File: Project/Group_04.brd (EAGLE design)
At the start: 100 x 80 mm, 29 parts, among them J1 POWER_JACKPTH_LOCK, U1 +12v

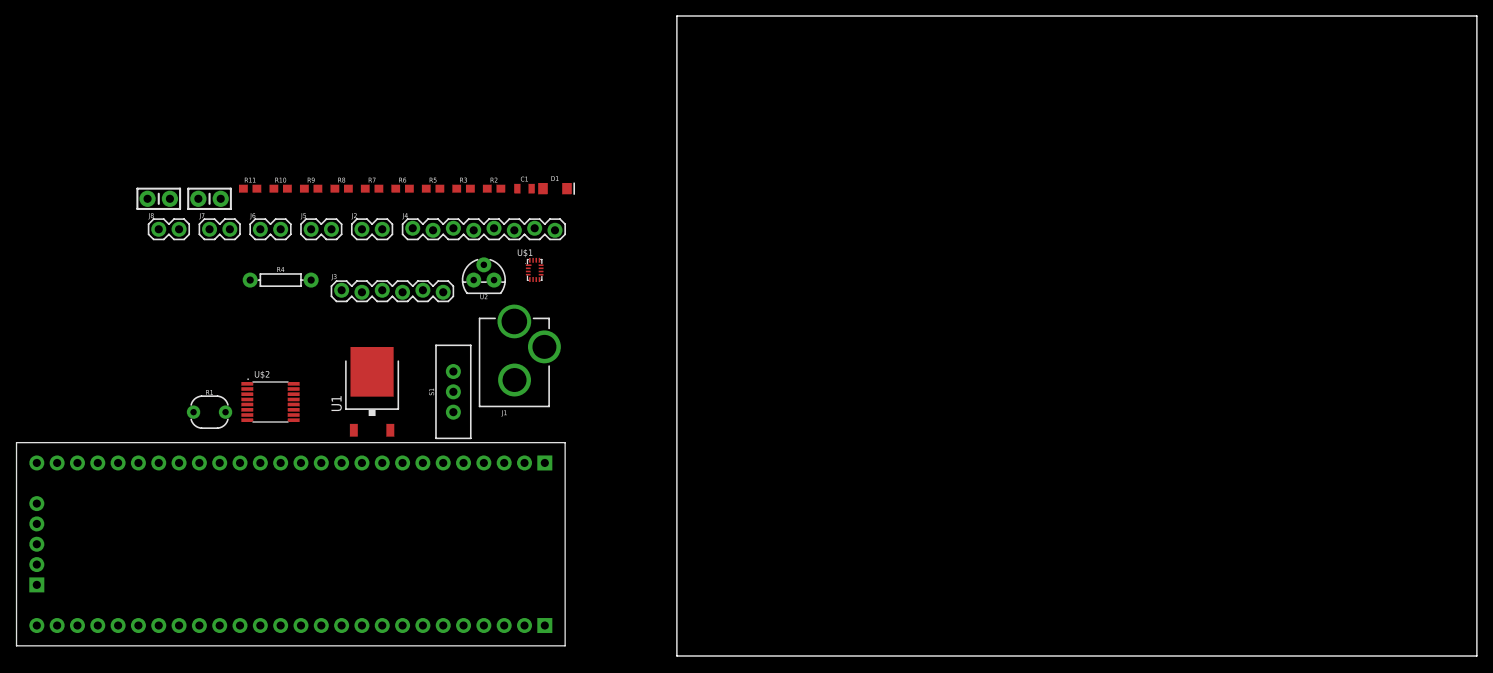
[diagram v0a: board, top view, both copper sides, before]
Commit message: components are positioned
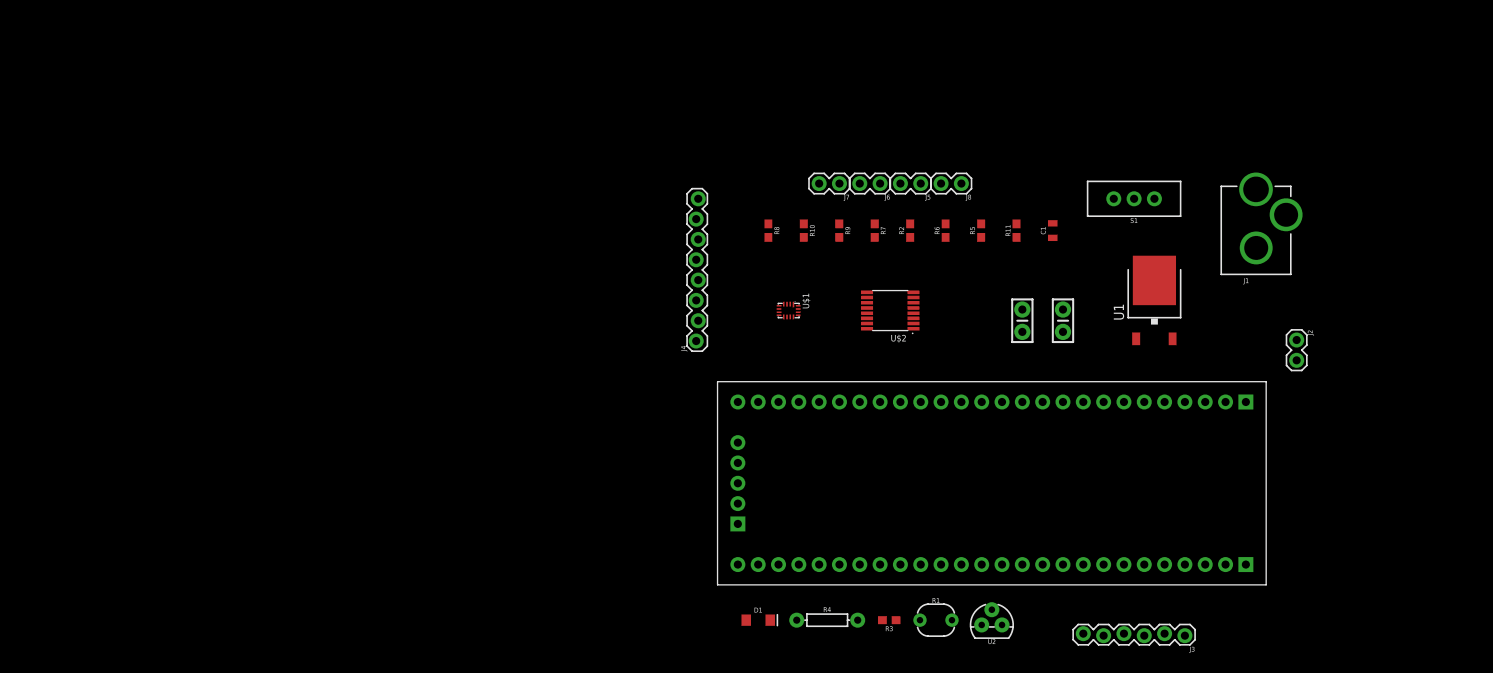
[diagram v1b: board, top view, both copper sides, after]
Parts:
- moved J2 117.7 mm to (77.5, 39.5), turned to 270 degrees
- moved C3 114.1 mm to (48.3, 41.9), turned to 270 degrees
- moved J3 113.9 mm to (63.5, 2.54), turned to 180 degrees
- moved C2 102.7 mm to (43.2, 41.9), turned to 270 degrees
- moved J8 100.5 mm to (35.6, 59.1), turned to 180 degrees
- moved U1 98.5 mm to (59.7, 44.5)
- moved R11 95.9 mm to (42.5, 53.2), turned to 90 degrees
- moved R1 94.5 mm to (32.4, 4.48)
- moved J1 94.2 mm to (72.4, 44.5)
- moved S1 88.4 mm to (57.1, 57.1), turned to 90 degrees
- moved U$3 88.0 mm to (40.6, 22.9)
- moved R4 80.5 mm to (18.8, 4.48)
- moved J7 78.9 mm to (20.3, 59.1), turned to 180 degrees
- moved U$2 78.3 mm to (26.7, 43.2), turned to 180 degrees
- moved J6 77.7 mm to (25.4, 59.1), turned to 180 degrees
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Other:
- board outline removed

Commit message: routed
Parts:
- moved U2 1.56 mm to (40.8, 4.44), turned to 90 degrees
- moved R4 0.96 mm to (19.7, 4.44)
- moved R3 0.76 mm to (27.3, 4.44), turned to 90 degrees
- moved R1 0.57 mm to (33.0, 4.44)
- moved D1 0.26 mm to (10.4, 4.44)
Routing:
- net 5V: track 0.00 -> 254.5 mm, vias 0 -> 2
- net I2C_A2: track 0.00 -> 34.9 mm
- net I2C_A0: track 0.00 -> 34.9 mm, vias 0 -> 2
- net I2C_A1: track 0.00 -> 31.9 mm
- net I2C_SCL_3: track 0.00 -> 30.9 mm, vias 0 -> 2
- net I2C_SDA_0: track 0.00 -> 28.7 mm, vias 0 -> 2
- net 12V: track 0.00 -> 26.6 mm
- net I2C_SDA_3: track 0.00 -> 24.9 mm, vias 0 -> 2
- net MUX_OUT: track 0.00 -> 23.7 mm, vias 0 -> 2
- net I2C_SCL_0: track 0.00 -> 23.3 mm, vias 0 -> 2
- net I2C_SCL_1: track 0.00 -> 20.8 mm, vias 0 -> 2
- net I2C_SDA_1: track 0.00 -> 20.7 mm, vias 0 -> 2
- net I2C_SCL_2: track 0.00 -> 20.0 mm, vias 0 -> 2
- net I2C_SDA: track 0.00 -> 18.2 mm, vias 0 -> 2
- net N$10: track 0.00 -> 17.9 mm
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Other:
- board outline added: 80 x 62.2 mm

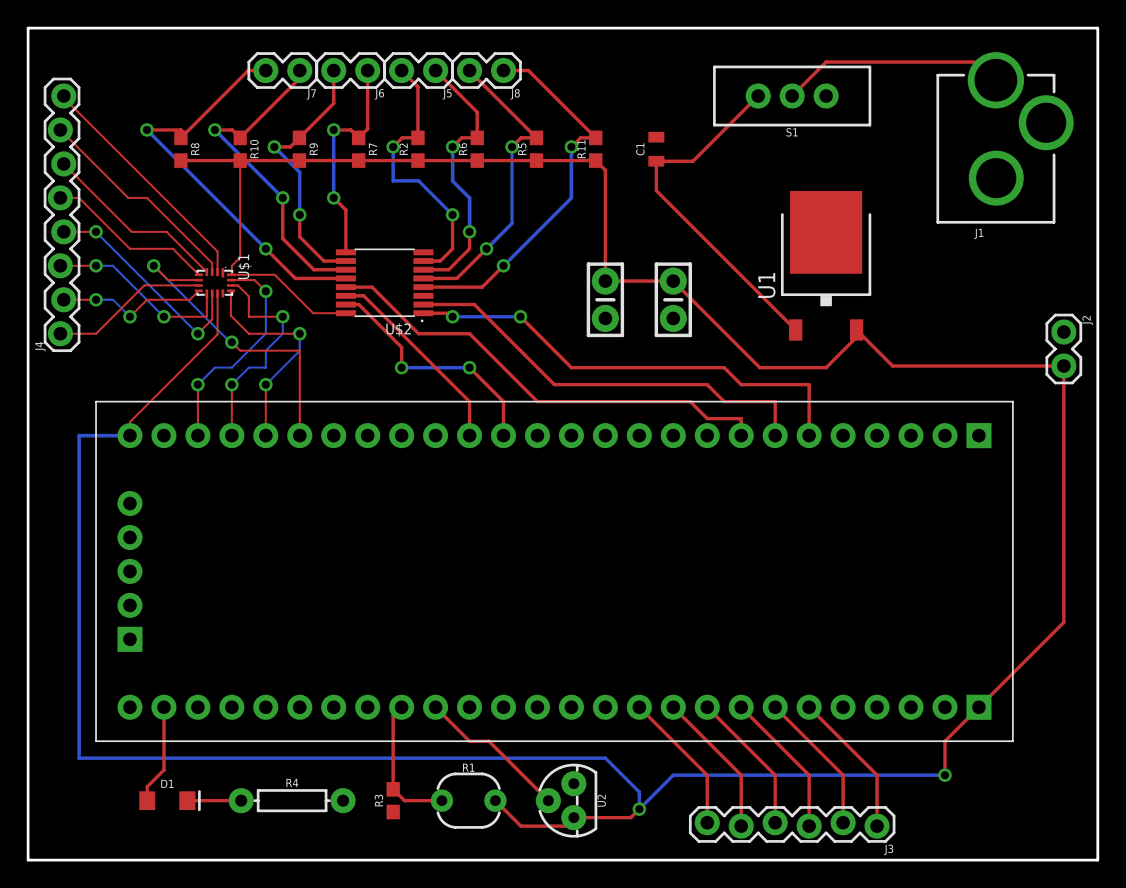
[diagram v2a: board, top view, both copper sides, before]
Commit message: copper pour added
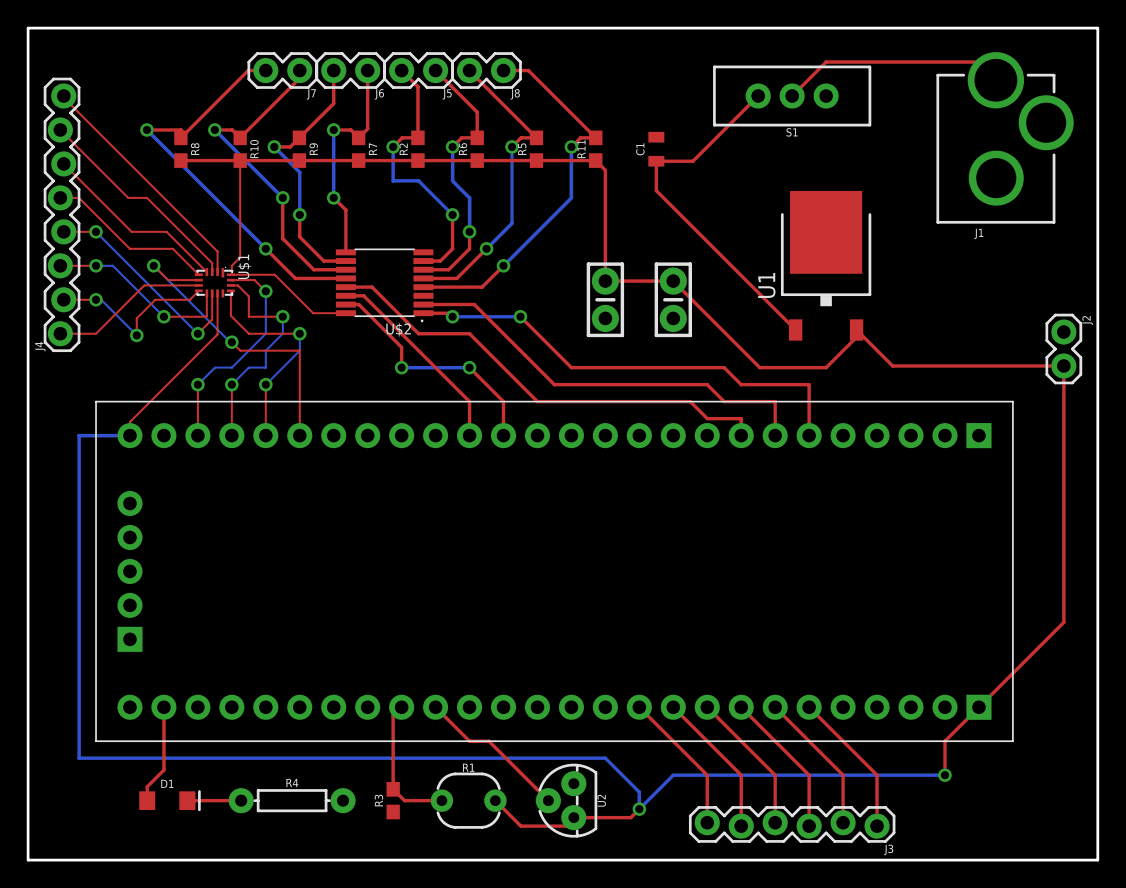
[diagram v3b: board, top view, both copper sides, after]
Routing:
- net N$16: track 11.4 -> 13.3 mm
- added copper zone on layer 1, net GND
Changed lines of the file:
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@@
 <wire x1="80.01" y1="62.23" x2="0" y2="62.23" width="0.2032" layer="20"/>
 <wire x1="0" y1="62.23" x2="0" y2="0" width="0.2032" layer="20"/>
+<dimension x1="0" y1="0" x2="80.01" y2="0" x3="40.005" y3="-3.81" textsize="1.778" layer="51" visible="yes"/>
+<dimension x1="0" y1="0" x2="0" y2="62.23" x3="-2.54" y3="31.115" textsize="1.778" layer="51" visible="yes"/>
 </plain>
 <attributes>
@@
 <contactref element="U$3" pad="28"/>
 <contactref element="R3" pad="1"/>
-<wire x1="72.4154" y1="51.007" x2="76.1516" y2="55.15" width="0" layer="19" extent="1-1"/>
-<wire x1="77.47" y1="39.497" x2="72.4154" y2="51.007" width="0" layer="19" extent="1-1"/>
-<wire x1="59.69" y1="46.95" x2="72.4154" y2="51.007" width="0" layer="19" extent="1-1"/>
-<wire x1="48.26" y1="40.513" x2="59.69" y2="46.95" width="0" layer="19" extent="1-1"/>
-<wire x1="43.18" y1="40.513" x2="48.26" y2="40.513" width="0" layer="19" extent="1-1"/>
-<wire x1="46.99" y1="54.0709375" x2="48.26" y2="40.513" width="0" layer="19" extent="1-1"/>
-<wire x1="29.57" y1="42.205" x2="43.18" y2="40.513" width="0" layer="19" extent="1-1"/>
-<wire x1="29.57" y1="45.455" x2="29.57" y2="42.205" width="0" layer="19" extent="1-1"/>
-<wire x1="14.57" y1="42.38" x2="29.57" y2="42.205" width="0" layer="19" extent="1-1"/>
-<wire x1="10.16" y1="31.75" x2="14.57" y2="42.38" width="0" layer="19" extent="1-1"/>
-<wire x1="68.58" y1="11.43" x2="77.47" y2="39.497" width="0" layer="19" extent="1-1"/>
-<wire x1="40.8199125" y1="5.714996875" x2="68.58" y2="11.43" width="0" layer="19" extent="1-1"/>
-<wire x1="27.30615625" y1="3.594953125" x2="40.8199125" y2="5.714996875" width="0" layer="19" extent="1-1"/>
-<wire x1="23.558178125" y1="4.444953125" x2="27.30615625" y2="3.594953125" width="0" layer="19" extent="1-1"/>
+<polygon width="0.1524" layer="1">
+<vertex x="0" y="0"/>
+<vertex x="80.01" y="0"/>
+<vertex x="80.01" y="62.23"/>
+<vertex x="0" y="62.23"/>
+</polygon>
 </signal>
 <signal name="N$1">
@@
 <wire x1="2.667" y1="41.91" x2="5.08" y2="41.91" width="0.1524" layer="1"/>
 <via x="5.08" y="41.91" extent="1-16" drill="0.6096"/>
-<wire x1="5.08" y1="41.91" x2="6.35" y2="41.91" width="0.1524" layer="16"/>
-<wire x1="6.35" y1="41.91" x2="7.62" y2="40.64" width="0.1524" layer="16"/>
-<via x="7.62" y="40.64" extent="1-16" drill="0.6096"/>
-<wire x1="7.62" y1="40.64" x2="8.89" y2="41.91" width="0.1524" layer="1"/>
+<wire x1="5.08" y1="41.91" x2="5.461" y2="41.91" width="0.1524" layer="16"/>
+<wire x1="5.461" y1="41.91" x2="8.128" y2="39.243" width="0.1524" layer="16"/>
+<via x="8.128" y="39.243" extent="1-16" drill="0.6096"/>
+<wire x1="9.525" y1="41.91" x2="8.128" y2="40.513" width="0.1524" layer="1"/>
+<wire x1="8.128" y1="39.243" x2="8.128" y2="40.513" width="0.1524" layer="1"/>
 <wire x1="12.1" y1="41.91" x2="12.77" y2="42.58" width="0.1524" layer="1"/>
-<wire x1="8.89" y1="41.91" x2="12.1" y2="41.91" width="0.1524" layer="1"/>
+<wire x1="9.525" y1="41.91" x2="12.1" y2="41.91" width="0.1524" layer="1"/>
 </signal>
 <signal name="N$17">

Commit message: V5,GND copper pours modified and PCB scaled down
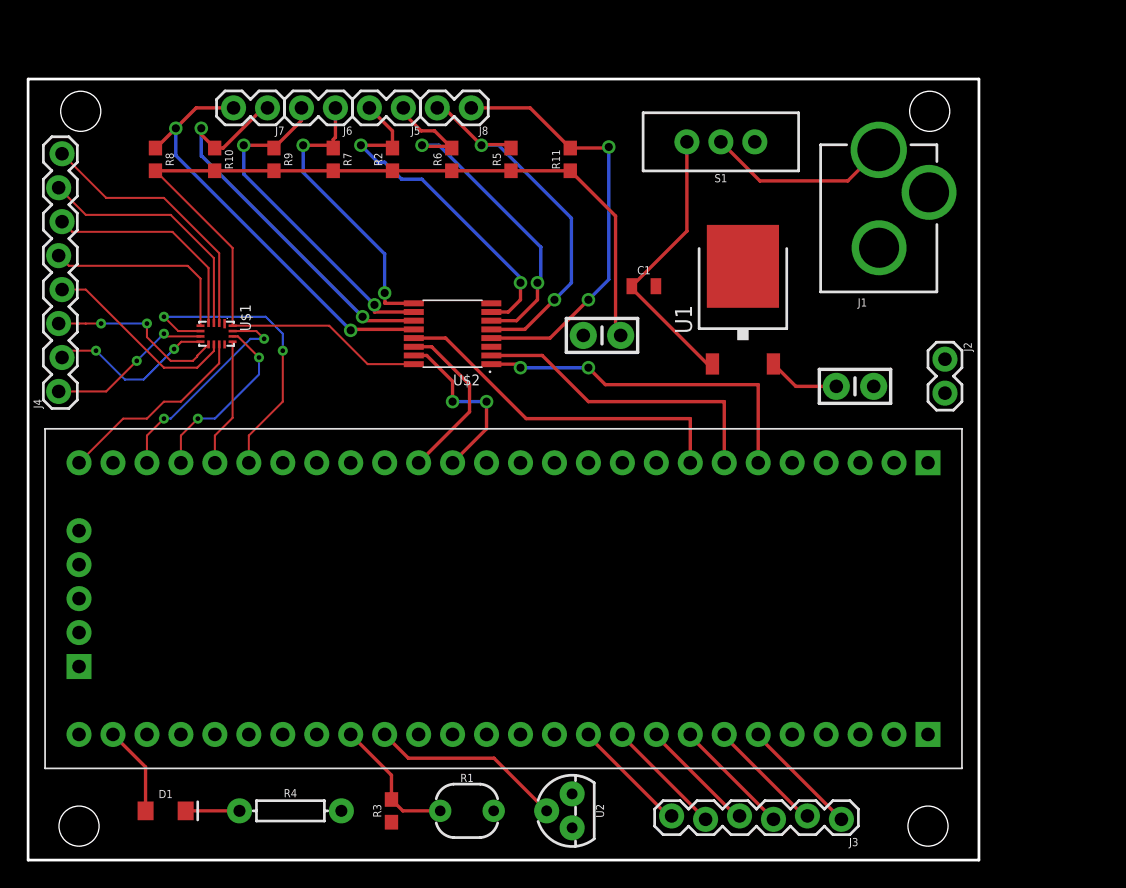
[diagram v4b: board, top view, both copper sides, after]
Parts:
- moved C3 15.1 mm to (61.8, 35.4), turned to 0 degrees
- moved C1 10.3 mm to (46.1, 42.9), turned to 0 degrees
- moved J1 10.2 mm to (63.6, 39.2)
- moved J2 9.12 mm to (68.6, 37.5)
- moved U1 6.72 mm to (53.5, 41.9)
- moved U$2 6.35 mm to (31.8, 39.4)
- moved S1 6.34 mm to (51.8, 53.7)
- moved J4 4.32 mm to (2.41, 35.1)
- moved U$3 4.32 mm to (36.8, 20.8)
- moved U$1 3.81 mm to (14.1, 39.4)
- moved J8 3.69 mm to (33.1, 56.3)
- moved J5 3.69 mm to (28.1, 56.3)
- moved J6 3.69 mm to (23.0, 56.3)
- moved J7 3.69 mm to (17.9, 56.3)
- moved J3 2.71 mm to (60.8, 3.05)
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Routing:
- net 5V: track 254.5 -> 94.0 mm, vias 2 -> 0
- net I2C_A2: track 34.9 -> 26.5 mm
- net I2C_A1: track 31.9 -> 23.4 mm
- net I2C_A0: track 34.9 -> 26.4 mm
- net I2C_SDA_1: track 20.7 -> 27.6 mm
- net MUX_A2: track 16.2 -> 9.60 mm, vias 2 -> 0
- net I2C_SCL_2: track 20.0 -> 26.0 mm
- net I2C_SCL_1: track 20.8 -> 26.4 mm
- net 12V: track 26.6 -> 21.0 mm
- net I2C_SDA_3: track 24.9 -> 30.3 mm
- net I2C_SDA_2: track 17.0 -> 22.0 mm
- net I2C_SCL_0: track 23.3 -> 28.2 mm
- net I2C_SDA: track 18.2 -> 13.4 mm
- net I2C_SDA_0: track 28.7 -> 32.1 mm
- net MUX_A1: track 17.0 -> 13.7 mm
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- added copper zone on layer 16, net 5V
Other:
- board size 80 x 62.2 mm -> 71.1 x 58.4 mm

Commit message: one warning fixed, silkscreen and dru file
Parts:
- moved R5 1.27 mm to (36.1, 51.1)
- moved U1 1.27 mm to (53.5, 43.2)
- moved C2 1.27 mm to (44.2, 39.2)
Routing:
- net 5V: track 94.0 -> 96.0 mm
- net MUX_A2: track 9.60 -> 10.7 mm
- net MUX_OUT: track 23.3 -> 23.9 mm
- net MUX_A0: track 16.4 -> 17.0 mm
- net 12V: track 21.0 -> 20.5 mm
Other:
- board text added: "+12V"
- board text added: "0.33uF"
- board text added: "4.7k"
- board text added: "5V"
- board text added: "BLUE LED"
- board text added: "C1"
- board text added: "GND"
- board text added: "PHOTOCELL"
- board text added: "POWER_JACKPTH"
- board text added: "R1"
- board text added: "R3"
- board text added: "R4"
- board text added: "TCA9546ASMD"
- board text added: "TEMP_SENS"
- board text added: "TMUX1208"
